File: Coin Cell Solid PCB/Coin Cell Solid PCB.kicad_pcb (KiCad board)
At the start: 4 copper layers, 50 x 50 mm, 51 parts, among them J1 0473461001, J4 UJ2-MIBV-4-SMT-TR-67, Q2 Q_PMOS_GSD, SW1 5136TR, U1 BQ21040DBVR, U2 TLV74010PDBVR, U3 LTC6992CS6-3#TRMPBF, U4 AP2502KTR-G1, U5 AP2502KTR-G1, U6 LTC2954CTS8-1#TRMPBF

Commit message: 0 DRC on Solid PCB
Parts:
- TP7: footprint TestPoint:TestPoint_Pad_D1.0mm -> Dylan Library:Harwin_S2761-46R
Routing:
- net VDD: track 28.2 -> 29.6 mm
- net GND: track 12.0 -> 13.1 mm

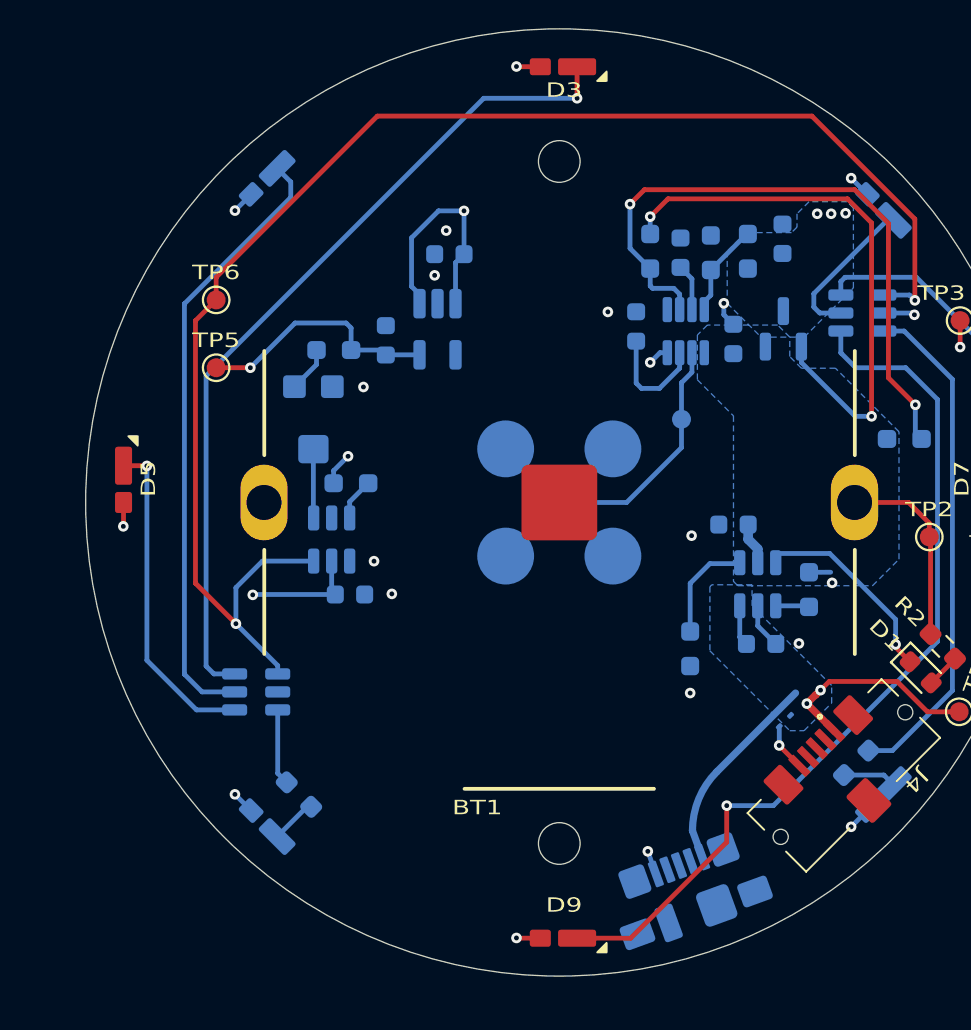
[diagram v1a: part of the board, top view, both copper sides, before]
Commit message: Added silk screen final touches, all PCBs 0.8mm, updated Fmod,
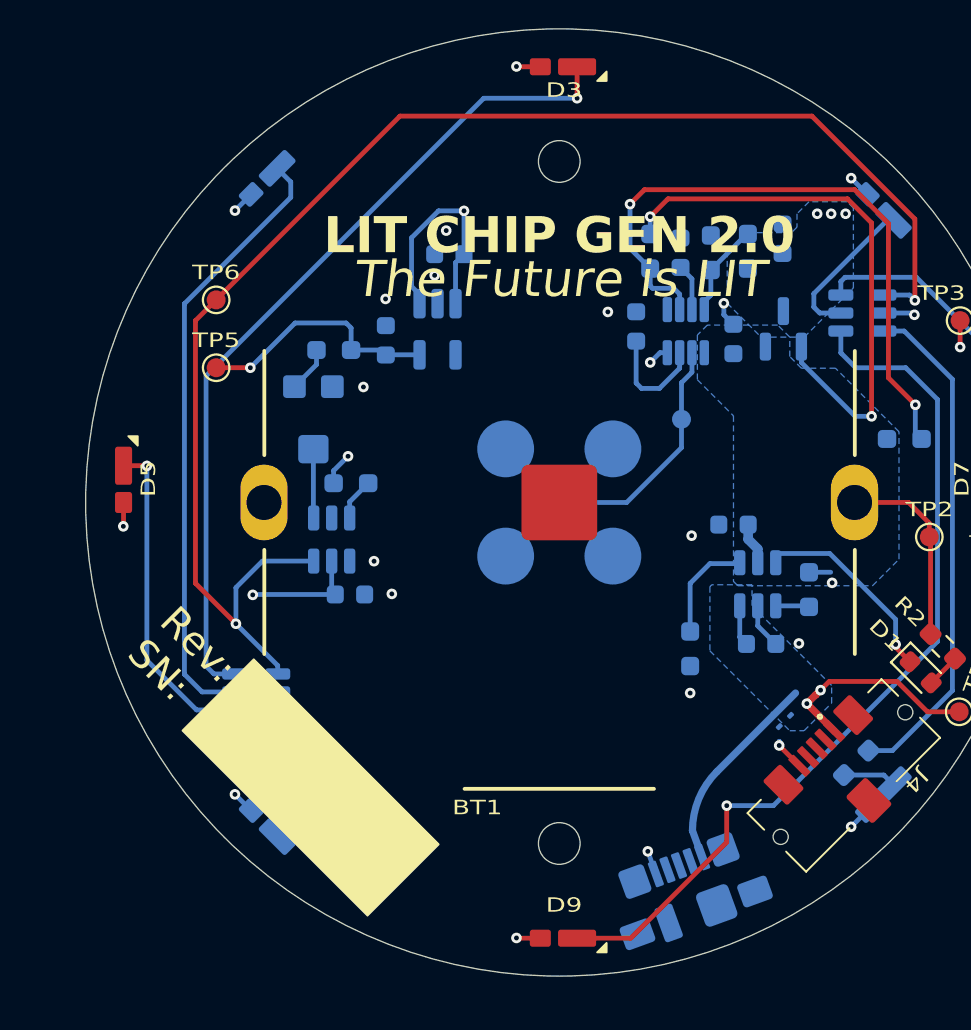
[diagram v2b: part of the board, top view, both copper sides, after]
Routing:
- net GND: track 13.1 -> 12.4 mm, vias 16 -> 17
- net /PWM_OUT: track 78.5 -> 77.8 mm
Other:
- board text added: "LIT CHIP GEN 2.0"
- board text added: "Rev: SN:"
- board text added: "The Future is LIT"
